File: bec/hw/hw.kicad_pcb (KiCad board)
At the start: 2 copper layers, 35.5 x 35.5 mm, 12 parts, among them U1 STSPIN32F0, U2 STSPIN32F0, U3 STSPIN32F0, U4 STSPIN32F0

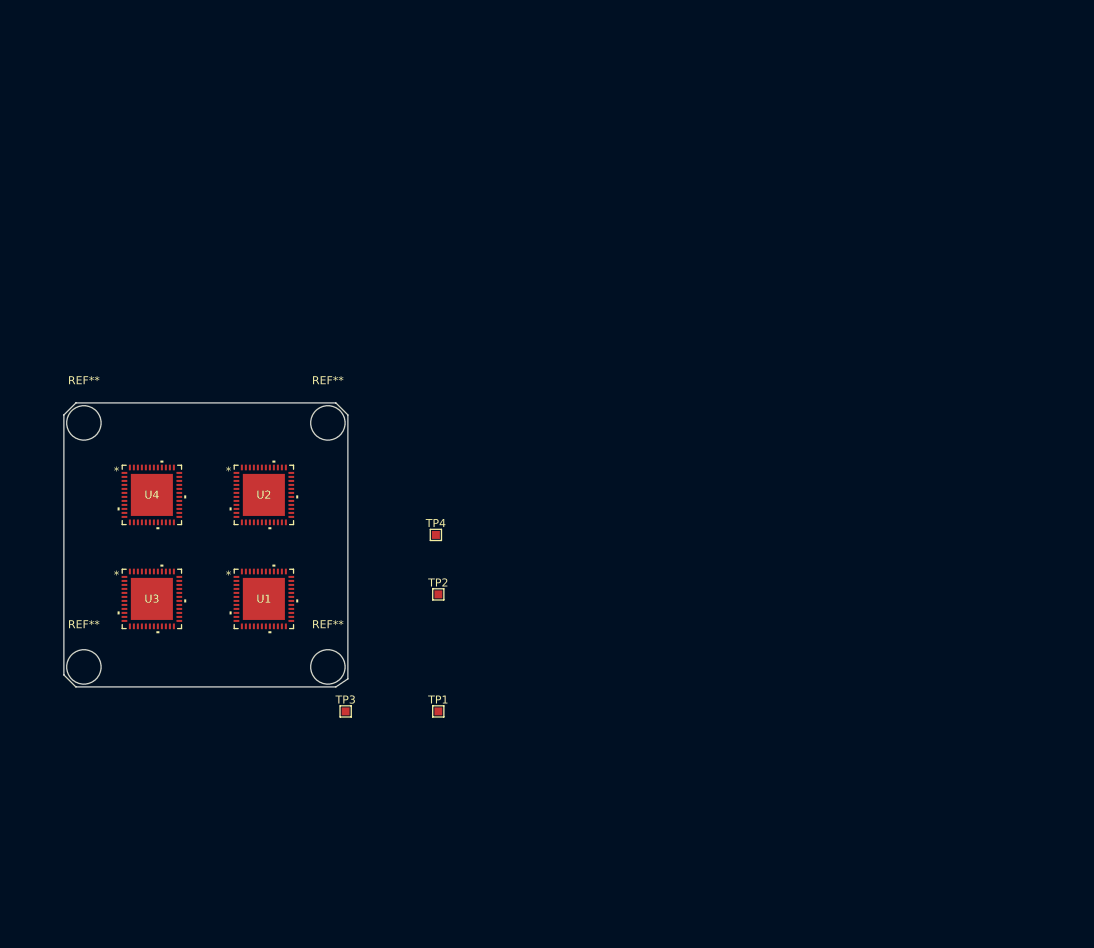
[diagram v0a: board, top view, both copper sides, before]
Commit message: Added motor phase half bridges
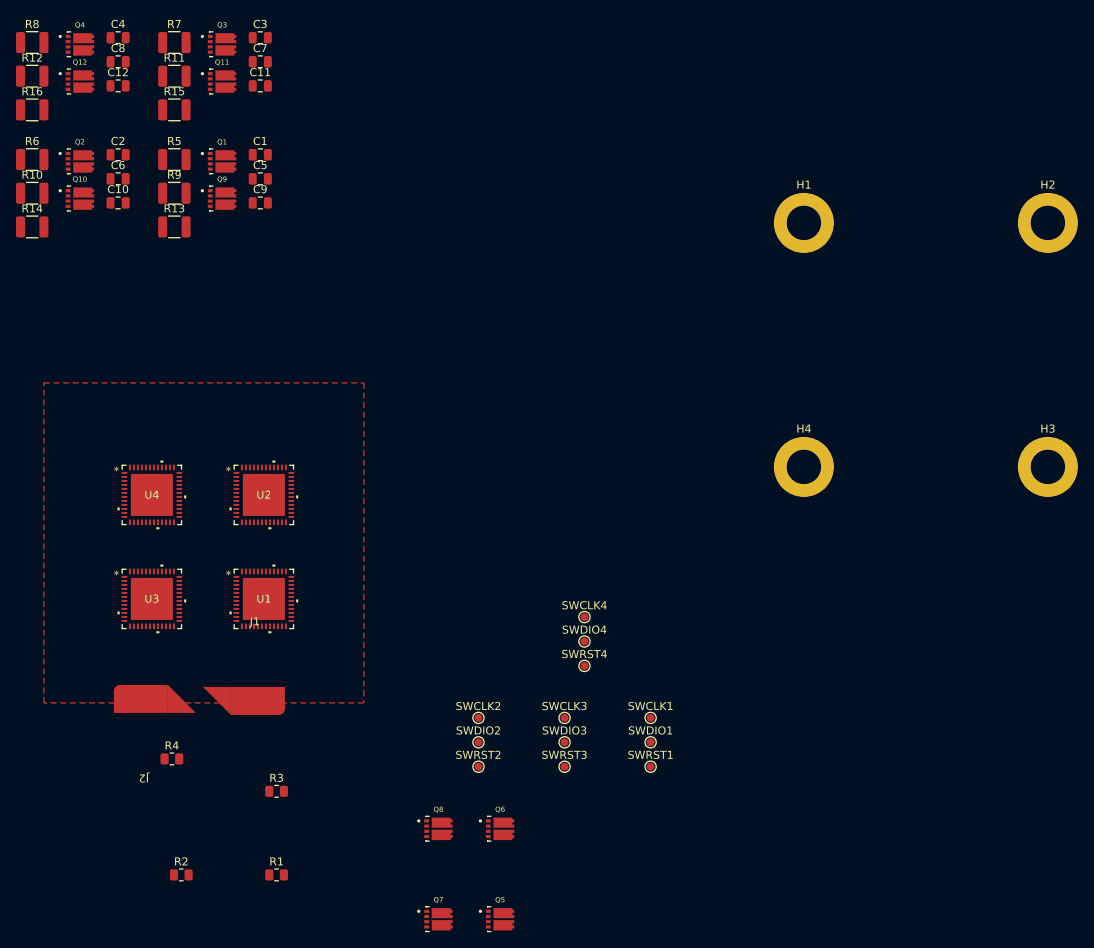
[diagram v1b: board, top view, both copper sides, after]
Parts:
- removed REF** (x4): MountingHole_4.3mm_M4, MountingHole:MountingHole_4.3mm_M4
- removed TP1, TP2, TP3, TP4: TestPoint, TestPoint:TestPoint_Pad_1.0x1.0mm
- added C1: 10u, Capacitor_SMD:C_0805_2012Metric, F.Cu at (132.1, 41.5)
- added C10: 10u, Capacitor_SMD:C_0805_2012Metric, F.Cu at (114.3, 47.5)
- added C11: 10u, Capacitor_SMD:C_0805_2012Metric, F.Cu at (132.1, 32.9)
- added C12: 10u, Capacitor_SMD:C_0805_2012Metric, F.Cu at (114.3, 32.9)
- added C2: 10u, Capacitor_SMD:C_0805_2012Metric, F.Cu at (114.3, 41.5)
- added C3: 10u, Capacitor_SMD:C_0805_2012Metric, F.Cu at (132.1, 26.9)
- added C4: 10u, Capacitor_SMD:C_0805_2012Metric, F.Cu at (114.3, 26.9)
- added C5: 10u, Capacitor_SMD:C_0805_2012Metric, F.Cu at (132.1, 44.5)
- added C6: 10u, Capacitor_SMD:C_0805_2012Metric, F.Cu at (114.3, 44.5)
- added C7: 10u, Capacitor_SMD:C_0805_2012Metric, F.Cu at (132.1, 29.9)
- added C8: 10u, Capacitor_SMD:C_0805_2012Metric, F.Cu at (114.3, 29.9)
- added C9: 10u, Capacitor_SMD:C_0805_2012Metric, F.Cu at (132.1, 47.5)
- added H1: MountingHole_Pad, MountingHole:MountingHole_4.3mm_M4_DIN965_Pad, F.Cu at (200.0, 50.0)
- added H2: MountingHole_Pad, MountingHole:MountingHole_4.3mm_M4_DIN965_Pad, F.Cu at (230.5, 50.0)
- added H3: MountingHole_Pad, MountingHole:MountingHole_4.3mm_M4_DIN965_Pad, F.Cu at (230.5, 80.5)
- added H4: MountingHole_Pad, MountingHole:MountingHole_4.3mm_M4_DIN965_Pad, F.Cu at (200.0, 80.5)
- added J1: Conn_01x01_Pin, CastellatedConnectors:Battery Terminal, F.Cu at (131.4, 109.8)
- added J2: Conn_01x01_Pin, CastellatedConnectors:Battery Terminal, F.Cu at (117.5, 109.5)
- added Q1: TSM200N03DPQ33_RGG, Snapeda:TSM200N03DPQ33_RGG_TRANS_TSM200N03DPQ33_RGG, F.Cu at (127.3, 42.3)
- added Q10: TSM200N03DPQ33_RGG, Snapeda:TSM200N03DPQ33_RGG_TRANS_TSM200N03DPQ33_RGG, F.Cu at (109.5, 47.0)
- added Q11: TSM200N03DPQ33_RGG, Snapeda:TSM200N03DPQ33_RGG_TRANS_TSM200N03DPQ33_RGG, F.Cu at (127.3, 32.3)
- added Q12: TSM200N03DPQ33_RGG, Snapeda:TSM200N03DPQ33_RGG_TRANS_TSM200N03DPQ33_RGG, F.Cu at (109.5, 32.3)
- added Q2: TSM200N03DPQ33_RGG, Snapeda:TSM200N03DPQ33_RGG_TRANS_TSM200N03DPQ33_RGG, F.Cu at (109.5, 42.3)
- added Q3: TSM200N03DPQ33_RGG, Snapeda:TSM200N03DPQ33_RGG_TRANS_TSM200N03DPQ33_RGG, F.Cu at (127.3, 27.7)
- added Q4: TSM200N03DPQ33_RGG, Snapeda:TSM200N03DPQ33_RGG_TRANS_TSM200N03DPQ33_RGG, F.Cu at (109.5, 27.7)
- added Q5: TSM200N03DPQ33_RGG, Snapeda:TSM200N03DPQ33_RGG_TRANS_TSM200N03DPQ33_RGG, F.Cu at (162.0, 137.0)
- added Q6: TSM200N03DPQ33_RGG, Snapeda:TSM200N03DPQ33_RGG_TRANS_TSM200N03DPQ33_RGG, F.Cu at (162.0, 125.7)
- added Q7: TSM200N03DPQ33_RGG, Snapeda:TSM200N03DPQ33_RGG_TRANS_TSM200N03DPQ33_RGG, F.Cu at (154.3, 137.0)
- added Q8: TSM200N03DPQ33_RGG, Snapeda:TSM200N03DPQ33_RGG_TRANS_TSM200N03DPQ33_RGG, F.Cu at (154.3, 125.7)
- added Q9: TSM200N03DPQ33_RGG, Snapeda:TSM200N03DPQ33_RGG_TRANS_TSM200N03DPQ33_RGG, F.Cu at (127.3, 47.0)
- added R1: 10k, Resistor_SMD:R_0805_2012Metric, F.Cu at (134.1, 131.5)
- added R10: 10m, Resistor_SMD:R_1210_3225Metric, F.Cu at (103.5, 46.3)
- added R11: 10m, Resistor_SMD:R_1210_3225Metric, F.Cu at (121.3, 31.7)
- added R12: 10m, Resistor_SMD:R_1210_3225Metric, F.Cu at (103.5, 31.7)
- added R13: 10m, Resistor_SMD:R_1210_3225Metric, F.Cu at (121.3, 50.5)
- added R14: 10m, Resistor_SMD:R_1210_3225Metric, F.Cu at (103.5, 50.5)
- added R15: 10m, Resistor_SMD:R_1210_3225Metric, F.Cu at (121.3, 35.9)
- added R16: 10m, Resistor_SMD:R_1210_3225Metric, F.Cu at (103.5, 35.9)
- added R2: 10k, Resistor_SMD:R_0805_2012Metric, F.Cu at (122.2, 131.5)
- added R3: 10k, Resistor_SMD:R_0805_2012Metric, F.Cu at (134.1, 121.0)
- added R4: 10k, Resistor_SMD:R_0805_2012Metric, F.Cu at (121.0, 117.0)
- added R5: 10m, Resistor_SMD:R_1210_3225Metric, F.Cu at (121.3, 42.1)
- added R6: 10m, Resistor_SMD:R_1210_3225Metric, F.Cu at (103.5, 42.1)
- added R7: 10m, Resistor_SMD:R_1210_3225Metric, F.Cu at (121.3, 27.4)
- added R8: 10m, Resistor_SMD:R_1210_3225Metric, F.Cu at (103.5, 27.4)
- added R9: 10m, Resistor_SMD:R_1210_3225Metric, F.Cu at (121.3, 46.3)
- added SWCLK1: TestPoint, TestPoint:TestPoint_Pad_D1.0mm, F.Cu at (180.8, 111.9)
- added SWCLK2: TestPoint, TestPoint:TestPoint_Pad_D1.0mm, F.Cu at (159.3, 111.9)
- added SWCLK3: TestPoint, TestPoint:TestPoint_Pad_D1.0mm, F.Cu at (170.1, 111.9)
- added SWCLK4: TestPoint, TestPoint:TestPoint_Pad_D1.0mm, F.Cu at (172.6, 99.3)
- added SWDIO1: TestPoint, TestPoint:TestPoint_Pad_D1.0mm, F.Cu at (180.8, 114.9)
- added SWDIO2: TestPoint, TestPoint:TestPoint_Pad_D1.0mm, F.Cu at (159.3, 114.9)
- added SWDIO3: TestPoint, TestPoint:TestPoint_Pad_D1.0mm, F.Cu at (170.1, 114.9)
- added SWDIO4: TestPoint, TestPoint:TestPoint_Pad_D1.0mm, F.Cu at (172.6, 102.3)
- added SWRST1: TestPoint, TestPoint:TestPoint_Pad_D1.0mm, F.Cu at (180.8, 118.0)
- added SWRST2: TestPoint, TestPoint:TestPoint_Pad_D1.0mm, F.Cu at (159.3, 118.0)
- added SWRST3: TestPoint, TestPoint:TestPoint_Pad_D1.0mm, F.Cu at (170.1, 118.0)
- added SWRST4: TestPoint, TestPoint:TestPoint_Pad_D1.0mm, F.Cu at (172.6, 105.4)
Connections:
- U1 pad 25: unconnected-(U1-HSW-Pad25) -> /Motor Control Unit A/C_HIGH
- U1 pad 26: unconnected-(U1-OUTW-Pad26) -> /Motor Control Unit A/C_OUT
- U1 pad 27: unconnected-(U1-VBOOTW-Pad27) -> /Motor Control Unit A/C_BOOT
- U1 pad 28: unconnected-(U1-LSW-Pad28) -> /Motor Control Unit A/C_LOW
- U1 pad 29: unconnected-(U1-HSV-Pad29) -> /Motor Control Unit A/B_HIGH
- U1 pad 30: unconnected-(U1-OUTV-Pad30) -> /Motor Control Unit A/B_OUT
- U1 pad 31: unconnected-(U1-VBOOTV-Pad31) -> /Motor Control Unit A/B_BOOT
- U1 pad 32: unconnected-(U1-LSV-Pad32) -> /Motor Control Unit A/B_LOW
- U1 pad 33: unconnected-(U1-HSU-Pad33) -> /Motor Control Unit A/A_HIGH
- U1 pad 34: unconnected-(U1-OUTU-Pad34) -> /Motor Control Unit A/A_OUT
- U1 pad 35: unconnected-(U1-VBOOTU-Pad35) -> /Motor Control Unit A/A_BOOT
- U1 pad 36: unconnected-(U1-LSU-Pad36) -> /Motor Control Unit A/A_LOW
- U1 pad 37: unconnected-(U1-PA13_SWD_IO-Pad37) -> /Motor Control Unit A/SWDIO
- U1 pad 38: unconnected-(U1-PA14_SWD_CLK-Pad38) -> /Motor Control Unit A/SWCLK
- U1 pad 44: unconnected-(U1-GND-Pad44) -> GND
- U1 pad 49: unconnected-(U1-GND-Pad49) -> GND
- U1 pad 7: Net-(U1-NRST) -> /Motor Control Unit A/SWD_NRST
- U2 pad 25: unconnected-(U2-HSW-Pad25) -> /Motor Control Unit B/C_HIGH
- U2 pad 26: unconnected-(U2-OUTW-Pad26) -> /Motor Control Unit B/C_OUT
- U2 pad 27: unconnected-(U2-VBOOTW-Pad27) -> /Motor Control Unit B/C_BOOT
- U2 pad 28: unconnected-(U2-LSW-Pad28) -> /Motor Control Unit B/C_LOW
- U2 pad 29: unconnected-(U2-HSV-Pad29) -> /Motor Control Unit B/B_HIGH
- U2 pad 30: unconnected-(U2-OUTV-Pad30) -> /Motor Control Unit B/B_OUT
- U2 pad 31: unconnected-(U2-VBOOTV-Pad31) -> /Motor Control Unit B/B_BOOT
- U2 pad 32: unconnected-(U2-LSV-Pad32) -> /Motor Control Unit B/B_LOW
- U2 pad 33: unconnected-(U2-HSU-Pad33) -> /Motor Control Unit B/A_HIGH
- U2 pad 34: unconnected-(U2-OUTU-Pad34) -> /Motor Control Unit B/A_OUT
- U2 pad 35: unconnected-(U2-VBOOTU-Pad35) -> /Motor Control Unit B/A_BOOT
- U2 pad 36: unconnected-(U2-LSU-Pad36) -> /Motor Control Unit B/A_LOW
- U2 pad 37: unconnected-(U2-PA13_SWD_IO-Pad37) -> /Motor Control Unit B/SWDIO
- U2 pad 38: unconnected-(U2-PA14_SWD_CLK-Pad38) -> /Motor Control Unit B/SWCLK
- U2 pad 44: unconnected-(U2-GND-Pad44) -> GND
- U2 pad 49: unconnected-(U2-GND-Pad49) -> GND
- U2 pad 7: Net-(U2-NRST) -> /Motor Control Unit B/SWD_NRST
- U3 pad 25: unconnected-(U3-HSW-Pad25) -> /Motor Control Unit C/C_HIGH
- U3 pad 26: unconnected-(U3-OUTW-Pad26) -> /Motor Control Unit C/C_OUT
- U3 pad 27: unconnected-(U3-VBOOTW-Pad27) -> /Motor Control Unit C/C_BOOT
- U3 pad 28: unconnected-(U3-LSW-Pad28) -> /Motor Control Unit C/C_LOW
- U3 pad 29: unconnected-(U3-HSV-Pad29) -> /Motor Control Unit C/B_HIGH
- U3 pad 30: unconnected-(U3-OUTV-Pad30) -> /Motor Control Unit C/B_OUT
- U3 pad 31: unconnected-(U3-VBOOTV-Pad31) -> /Motor Control Unit C/B_BOOT
- U3 pad 32: unconnected-(U3-LSV-Pad32) -> /Motor Control Unit C/B_LOW
- U3 pad 33: unconnected-(U3-HSU-Pad33) -> /Motor Control Unit C/A_HIGH
- U3 pad 34: unconnected-(U3-OUTU-Pad34) -> /Motor Control Unit C/A_OUT
- U3 pad 35: unconnected-(U3-VBOOTU-Pad35) -> /Motor Control Unit C/A_BOOT
- U3 pad 36: unconnected-(U3-LSU-Pad36) -> /Motor Control Unit C/A_LOW
- U3 pad 37: unconnected-(U3-PA13_SWD_IO-Pad37) -> /Motor Control Unit C/SWDIO
- U3 pad 38: unconnected-(U3-PA14_SWD_CLK-Pad38) -> /Motor Control Unit C/SWCLK
- U3 pad 44: unconnected-(U3-GND-Pad44) -> GND
- U3 pad 49: unconnected-(U3-GND-Pad49) -> GND
- U3 pad 7: Net-(U3-NRST) -> /Motor Control Unit C/SWD_NRST
- U4 pad 25: unconnected-(U4-HSW-Pad25) -> /Motor Control Unit D/C_HIGH
- U4 pad 26: unconnected-(U4-OUTW-Pad26) -> /Motor Control Unit D/C_OUT
- U4 pad 27: unconnected-(U4-VBOOTW-Pad27) -> /Motor Control Unit D/C_BOOT
- U4 pad 28: unconnected-(U4-LSW-Pad28) -> /Motor Control Unit D/C_LOW
- U4 pad 29: unconnected-(U4-HSV-Pad29) -> /Motor Control Unit D/B_HIGH
- U4 pad 30: unconnected-(U4-OUTV-Pad30) -> /Motor Control Unit D/B_OUT
- U4 pad 31: unconnected-(U4-VBOOTV-Pad31) -> /Motor Control Unit D/B_BOOT
- U4 pad 32: unconnected-(U4-LSV-Pad32) -> /Motor Control Unit D/B_LOW
- U4 pad 33: unconnected-(U4-HSU-Pad33) -> /Motor Control Unit D/A_HIGH
- U4 pad 34: unconnected-(U4-OUTU-Pad34) -> /Motor Control Unit D/A_OUT
- U4 pad 35: unconnected-(U4-VBOOTU-Pad35) -> /Motor Control Unit D/A_BOOT
- U4 pad 36: unconnected-(U4-LSU-Pad36) -> /Motor Control Unit D/A_LOW
- U4 pad 37: unconnected-(U4-PA13_SWD_IO-Pad37) -> /Motor Control Unit D/SWDIO
- U4 pad 38: unconnected-(U4-PA14_SWD_CLK-Pad38) -> /Motor Control Unit D/SWCLK
- U4 pad 44: unconnected-(U4-GND-Pad44) -> GND
- U4 pad 49: unconnected-(U4-GND-Pad49) -> GND
- U4 pad 7: Net-(U4-NRST) -> /Motor Control Unit D/SWD_NRST
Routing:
- added copper zone on F.Cu, net GND
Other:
- board outline removed

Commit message: Added TPS54331 for 3.3v supply
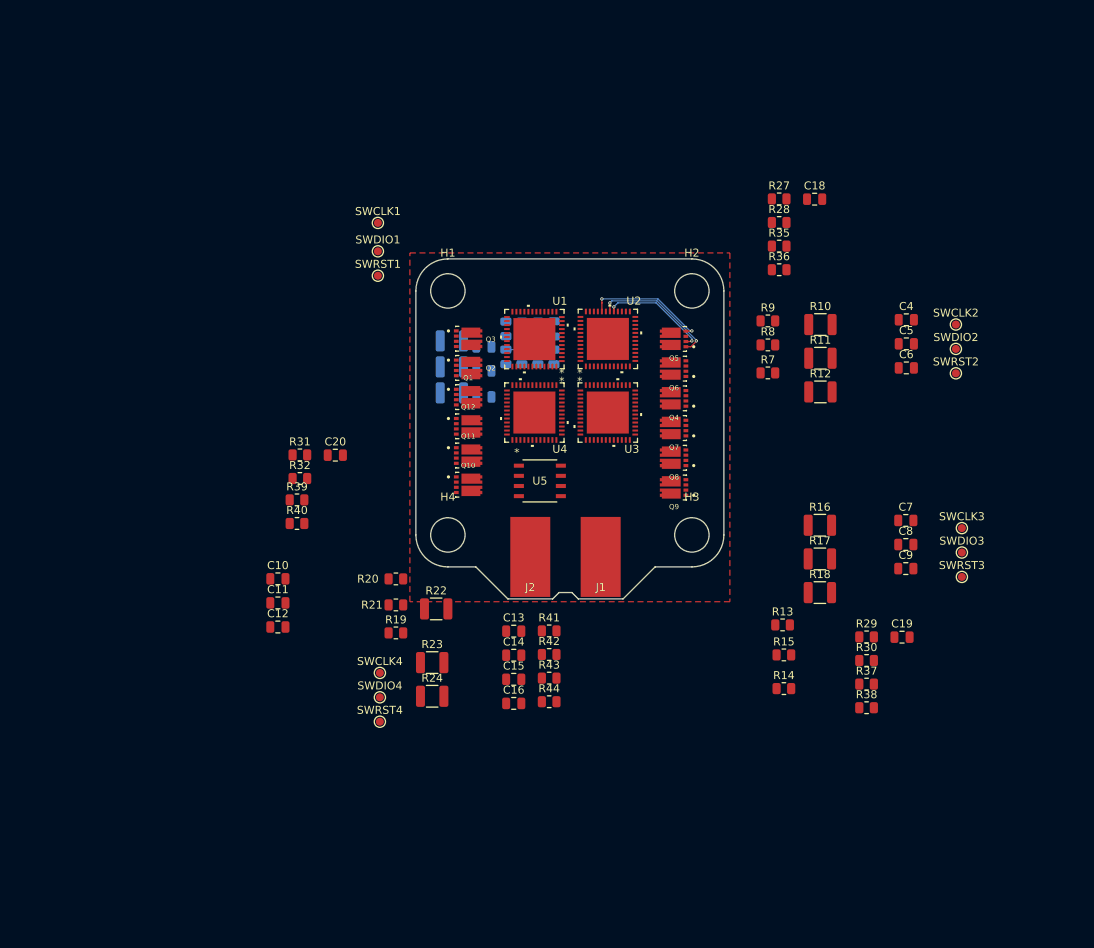
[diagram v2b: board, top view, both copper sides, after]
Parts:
- added C13: 47u, Capacitor_SMD:C_0805_2012Metric, F.Cu at (163.7, 101.0)
- added C14: C, Capacitor_SMD:C_0805_2012Metric, F.Cu at (163.7, 104.0)
- added C15: 47p, Capacitor_SMD:C_0805_2012Metric, F.Cu at (163.7, 107.0)
- added C16: 1n, Capacitor_SMD:C_0805_2012Metric, F.Cu at (163.7, 110.1)
- added C17: 10u, Capacitor_SMD:C_0805_2012Metric, B.Cu at (168.8, 63.2)
- added C18: 10u, Capacitor_SMD:C_0805_2012Metric, F.Cu at (201.3, 47.0)
- added C19: 10u, Capacitor_SMD:C_0805_2012Metric, F.Cu at (212.3, 101.8)
- added C20: 10u, Capacitor_SMD:C_0805_2012Metric, F.Cu at (141.4, 79.0)
- added R14: 1k, Resistor_SMD:R_0805_2012Metric, F.Cu at (197.5, 108.2)
- added R15: 100k, Resistor_SMD:R_0805_2012Metric, F.Cu at (197.5, 104.0)
- added R2: 1k, Resistor_SMD:R_0805_2012Metric, B.Cu at (162.8, 63.2)
- added R20: 1k, Resistor_SMD:R_0805_2012Metric, F.Cu at (149.0, 94.5)
- added R21: 100k, Resistor_SMD:R_0805_2012Metric, F.Cu at (149.0, 97.8)
- added R25: 1k, Resistor_SMD:R_0805_2012Metric, B.Cu at (162.8, 66.8)
- added R26: 100k, Resistor_SMD:R_0805_2012Metric, B.Cu at (164.8, 66.8)
- added R27: 1k, Resistor_SMD:R_0805_2012Metric, F.Cu at (196.9, 47.0)
- added R28: 100k, Resistor_SMD:R_0805_2012Metric, F.Cu at (196.9, 50.0)
- added R29: 1k, Resistor_SMD:R_0805_2012Metric, F.Cu at (207.8, 101.8)
- added R3: 100k, Resistor_SMD:R_0805_2012Metric, B.Cu at (164.8, 63.2)
- added R30: 100k, Resistor_SMD:R_0805_2012Metric, F.Cu at (207.8, 104.7)
- added R31: 1k, Resistor_SMD:R_0805_2012Metric, F.Cu at (137.0, 79.0)
- added R32: 100k, Resistor_SMD:R_0805_2012Metric, F.Cu at (137.0, 82.0)
- added R33: 1k, Resistor_SMD:R_0805_2012Metric, B.Cu at (166.8, 66.8)
- added R34: 100k, Resistor_SMD:R_0805_2012Metric, B.Cu at (168.8, 66.8)
- added R35: 1k, Resistor_SMD:R_0805_2012Metric, F.Cu at (196.9, 52.9)
- added R36: 100k, Resistor_SMD:R_0805_2012Metric, F.Cu at (196.9, 55.9)
- added R37: 1k, Resistor_SMD:R_0805_2012Metric, F.Cu at (207.8, 107.7)
- added R38: 100k, Resistor_SMD:R_0805_2012Metric, F.Cu at (207.8, 110.6)
- added R39: 1k, Resistor_SMD:R_0805_2012Metric, F.Cu at (136.6, 84.6)
- added R40: 100k, Resistor_SMD:R_0805_2012Metric, F.Cu at (136.6, 87.6)
- added R41: 10k, Resistor_SMD:R_0805_2012Metric, F.Cu at (168.2, 101.0)
- added R42: 2k2, Resistor_SMD:R_0805_2012Metric, F.Cu at (168.2, 104.0)
- added R43: 1k, Resistor_SMD:R_0805_2012Metric, F.Cu at (168.2, 106.9)
- added R44: 30k, Resistor_SMD:R_0805_2012Metric, F.Cu at (168.2, 109.8)
- added R8: 1k, Resistor_SMD:R_0805_2012Metric, F.Cu at (195.5, 65.2)
- added R9: 100k, Resistor_SMD:R_0805_2012Metric, F.Cu at (195.5, 62.2)
- added U5: TPS54331DR, Snapeda:D8, F.Cu at (167.0, 82.2)
- C1, R1: moved to B.Cu
- C2: renamed from C5; moved to B.Cu
- C3: renamed from C9; moved to B.Cu
- H1, H4: footprint MountingHole:MountingHole_4.3mm_M4_DIN965_Pad -> MountingHole:MountingHole_4.3mm_M4_DIN965
- H2: renamed from H3; footprint MountingHole:MountingHole_4.3mm_M4_DIN965_Pad -> MountingHole:MountingHole_4.3mm_M4_DIN965
- H3: renamed from H2; footprint MountingHole:MountingHole_4.3mm_M4_DIN965_Pad -> MountingHole:MountingHole_4.3mm_M4_DIN965
- J1, J2: footprint CastellatedConnectors:Battery Terminal -> Connector_Wire:SolderWirePad_1x01_SMD_5x10mm
- R10: renamed from R6; value 10m -> 1m
- R11: renamed from R10; value 10m -> 1m
- R12: renamed from R14; value 10m -> 1m
- R16: renamed from R7; value 10m -> 1m
- R17: renamed from R11; value 10m -> 1m
- R18: renamed from R15; value 10m -> 1m
- R22: renamed from R8; value 10m -> 1m
- R23: renamed from R12; value 10m -> 1m
- R24: renamed from R16; value 10m -> 1m
- R4: renamed from R5; value 10m -> 1m; moved to B.Cu
- R5: renamed from R9; value 10m -> 1m; moved to B.Cu
- R6: renamed from R13; value 10m -> 1m; moved to B.Cu
- moved C7 100.8 mm to (212.7, 87.2)
- moved C8 100.8 mm to (212.7, 90.2)
- moved C9 100.8 mm to (212.7, 93.2)
- moved R16 100.8 mm to (202.0, 87.8)
- moved R17 100.8 mm to (202.0, 92.0)
- moved R18 100.8 mm to (202.0, 96.2)
- moved C4 100.7 mm to (212.8, 62.1)
- moved C6 100.7 mm to (212.8, 68.1)
- moved R10 100.7 mm to (202.1, 62.7)
- moved R11 100.7 mm to (202.1, 66.9)
- moved R12 100.7 mm to (202.1, 71.1)
- moved C5 100.7 mm to (212.8, 65.1)
- moved R7 96.5 mm to (195.5, 68.8)
- moved R23 88.7 mm to (153.5, 105.0)
- moved R24 88.7 mm to (153.5, 109.2)
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- renumbered C4 to C10, C8 to C11, C2 to C4, C6 to C5, C10 to C6, C3 to C7, C7 to C8, C11 to C9, Q5 to Q1, Q8 to Q10, Q4 to Q11, Q1 to Q2, Q9 to Q3, Q6 to Q4, Q2 to Q5, Q10 to Q6, Q3 to Q8, Q11 to Q9, R3 to R13, R4 to R19, R2 to R7
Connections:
- Q12 pad 3: Net-(Q12-Pad3) -> /Motor Control Unit D/C_SHUNT
- Q3 pad 3: Net-(Q9-Pad3) -> /Motor Control Unit A/C_SHUNT
- Q6 pad 3: Net-(Q10-Pad3) -> /Motor Control Unit B/C_SHUNT
- Q9 pad 3: Net-(Q11-Pad3) -> /Motor Control Unit C/C_SHUNT
- R12 pad 1: Net-(Q10-Pad3) -> /Motor Control Unit B/C_SHUNT
- R18 pad 1: Net-(Q11-Pad3) -> /Motor Control Unit C/C_SHUNT
- R24 pad 1: Net-(Q12-Pad3) -> /Motor Control Unit D/C_SHUNT
- R6 pad 1: Net-(Q9-Pad3) -> /Motor Control Unit A/C_SHUNT
- U1 pad 10: unconnected-(U1-VDDA-Pad10) -> +3.3V
- U1 pad 21: unconnected-(U1-OP1O-Pad21) -> Net-(U1-OP1O)
- U1 pad 22: unconnected-(U1-OP1N-Pad22) -> Net-(U1-OP1N)
- U1 pad 23: unconnected-(U1-OP1P-Pad23) -> /Motor Control Unit A/A_SHUNT
- U1 pad 41: unconnected-(U1-OP2P-Pad41) -> /Motor Control Unit A/B_SHUNT
- U1 pad 42: unconnected-(U1-OP2N-Pad42) -> Net-(U1-OP2N)
- U1 pad 43: unconnected-(U1-OP2O-Pad43) -> Net-(U1-OP2O)
- U1 pad 45: unconnected-(U1-OP3P-Pad45) -> /Motor Control Unit A/C_SHUNT
- U1 pad 46: unconnected-(U1-OP3N-Pad46) -> Net-(U1-OP3N)
- U1 pad 47: unconnected-(U1-OP3O-Pad47) -> Net-(U1-OP3O)
- U1 pad 6: unconnected-(U1-VREG12-Pad6) -> +BATT
- U1 pad 8: unconnected-(U1-VM-Pad8) -> +BATT
- U1 pad 9: unconnected-(U1-SW-Pad9) -> +3.3V
- U2 pad 10: unconnected-(U2-VDDA-Pad10) -> +3.3V
- U2 pad 21: unconnected-(U2-OP1O-Pad21) -> Net-(U2-OP1O)
- U2 pad 22: unconnected-(U2-OP1N-Pad22) -> Net-(U2-OP1N)
- U2 pad 23: unconnected-(U2-OP1P-Pad23) -> /Motor Control Unit B/A_SHUNT
- U2 pad 41: unconnected-(U2-OP2P-Pad41) -> /Motor Control Unit B/B_SHUNT
- U2 pad 42: unconnected-(U2-OP2N-Pad42) -> Net-(U2-OP2N)
- U2 pad 43: unconnected-(U2-OP2O-Pad43) -> Net-(U2-OP2O)
- U2 pad 45: unconnected-(U2-OP3P-Pad45) -> /Motor Control Unit B/C_SHUNT
- U2 pad 46: unconnected-(U2-OP3N-Pad46) -> Net-(U2-OP3N)
- U2 pad 47: unconnected-(U2-OP3O-Pad47) -> Net-(U2-OP3O)
- U2 pad 6: unconnected-(U2-VREG12-Pad6) -> +BATT
- U2 pad 8: unconnected-(U2-VM-Pad8) -> +BATT
- U2 pad 9: unconnected-(U2-SW-Pad9) -> +3.3V
- U3 pad 10: unconnected-(U3-VDDA-Pad10) -> +3.3V
- U3 pad 21: unconnected-(U3-OP1O-Pad21) -> Net-(U3-OP1O)
- U3 pad 22: unconnected-(U3-OP1N-Pad22) -> Net-(U3-OP1N)
- U3 pad 23: unconnected-(U3-OP1P-Pad23) -> /Motor Control Unit C/A_SHUNT
- U3 pad 41: unconnected-(U3-OP2P-Pad41) -> /Motor Control Unit C/B_SHUNT
- U3 pad 42: unconnected-(U3-OP2N-Pad42) -> Net-(U3-OP2N)
- U3 pad 43: unconnected-(U3-OP2O-Pad43) -> Net-(U3-OP2O)
- U3 pad 45: unconnected-(U3-OP3P-Pad45) -> /Motor Control Unit C/C_SHUNT
- U3 pad 46: unconnected-(U3-OP3N-Pad46) -> Net-(U3-OP3N)
- U3 pad 47: unconnected-(U3-OP3O-Pad47) -> Net-(U3-OP3O)
- U3 pad 6: unconnected-(U3-VREG12-Pad6) -> +BATT
- U3 pad 8: unconnected-(U3-VM-Pad8) -> +BATT
- U3 pad 9: unconnected-(U3-SW-Pad9) -> +3.3V
- U4 pad 10: unconnected-(U4-VDDA-Pad10) -> +3.3V
- U4 pad 21: unconnected-(U4-OP1O-Pad21) -> Net-(U4-OP1O)
- U4 pad 22: unconnected-(U4-OP1N-Pad22) -> Net-(U4-OP1N)
- U4 pad 23: unconnected-(U4-OP1P-Pad23) -> /Motor Control Unit D/A_SHUNT
- U4 pad 41: unconnected-(U4-OP2P-Pad41) -> /Motor Control Unit D/B_SHUNT
- U4 pad 42: unconnected-(U4-OP2N-Pad42) -> Net-(U4-OP2N)
- U4 pad 43: unconnected-(U4-OP2O-Pad43) -> Net-(U4-OP2O)
- U4 pad 45: unconnected-(U4-OP3P-Pad45) -> /Motor Control Unit D/C_SHUNT
- U4 pad 46: unconnected-(U4-OP3N-Pad46) -> Net-(U4-OP3N)
- U4 pad 47: unconnected-(U4-OP3O-Pad47) -> Net-(U4-OP3O)
- U4 pad 6: unconnected-(U4-VREG12-Pad6) -> +BATT
- U4 pad 8: unconnected-(U4-VM-Pad8) -> +BATT
- U4 pad 9: unconnected-(U4-SW-Pad9) -> +3.3V
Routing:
- net /Motor Control Unit B/B_OUT: track 0.00 -> 15.7 mm, vias 0 -> 2
- net /Motor Control Unit B/B_LOW: track 0.00 -> 15.2 mm, vias 0 -> 2
- net /Motor Control Unit B/B_HIGH: track 0.00 -> 13.4 mm, vias 0 -> 2
- net Net-(U1-OP2N): track 0.00 -> 2.00 mm
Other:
- board outline added: 38.5 x 42.5 mm
